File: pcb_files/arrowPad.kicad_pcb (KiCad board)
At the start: 2 copper layers, 43 parts, among them J1 AudioJack3_Ground, J2 AudioJack3_Ground, K1 KEYSW, K10 KEYSW, K11 KEYSW, K12 KEYSW, K13 KEYSW, K14 KEYSW, K15 KEYSW, K16 KEYSW, K2 KEYSW, K3 KEYSW, K4 KEYSW, K5 KEYSW, K6 KEYSW, K7 KEYSW, K8 KEYSW, K9 KEYSW, U1 ProMicro, U2 NRF24L01_Breakout, U3 ADG417BN, U4 AMS1117-3.3, U5 ADG417BN, U6 ADG417BN

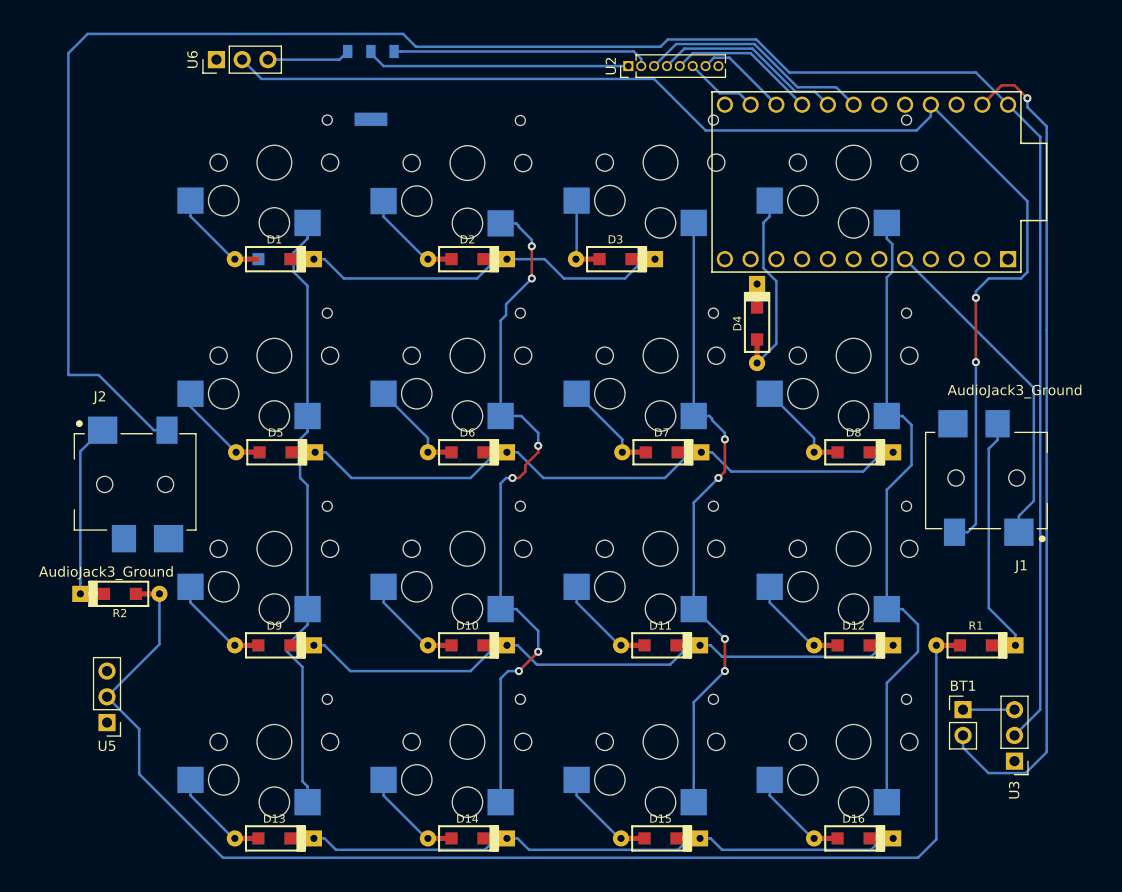
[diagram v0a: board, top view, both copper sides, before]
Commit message: ldo heat sink and edge cuts
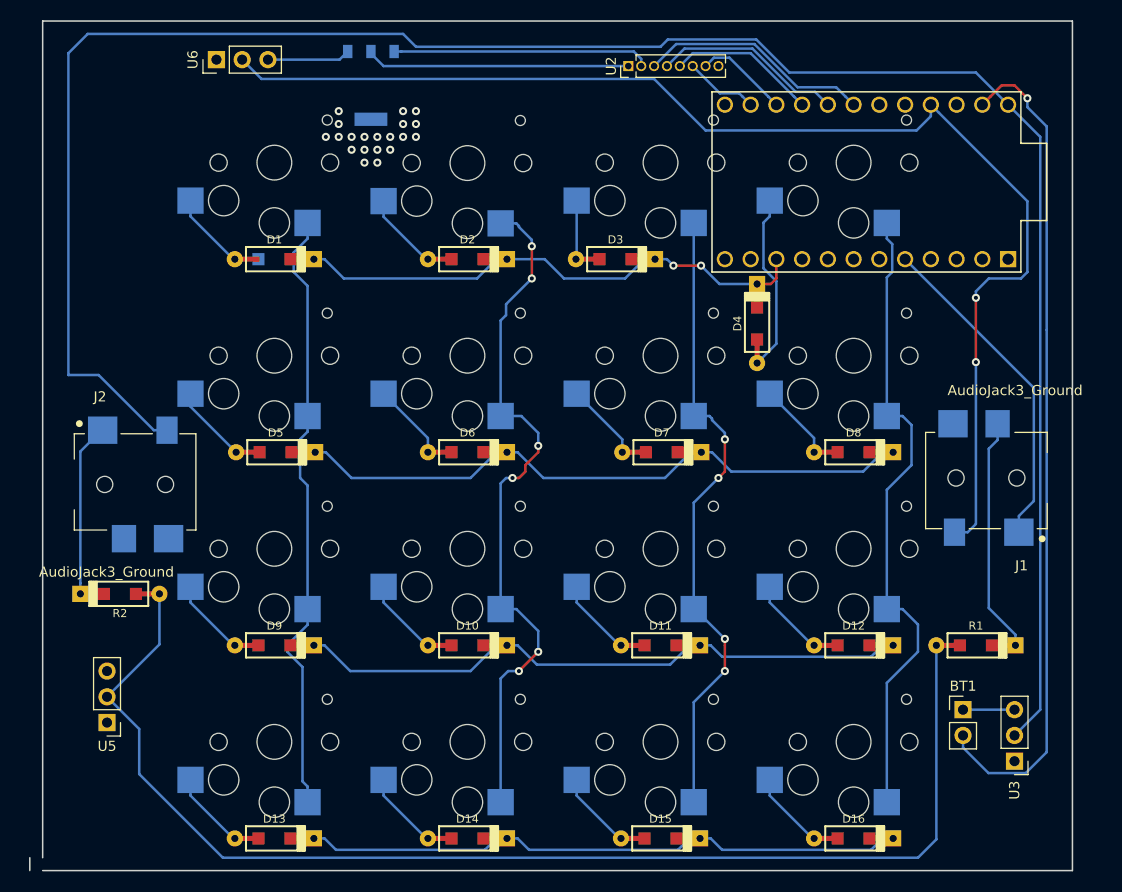
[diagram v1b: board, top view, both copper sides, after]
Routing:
- net /Row1: track 36.8 -> 51.9 mm, vias 0 -> 2
- net (no net): vias 0 -> 20
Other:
- board outline added: 102.9 x 83.8 mm
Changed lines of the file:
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@@
-(kicad_pcb (version 20171130) (host pcbnew "(5.0.0-3-g5ebb6b6)")
+(kicad_pcb (version 20171130) (host pcbnew "(5.0.1)-4")
   (general
     (thickness 1.6)
-    (drawings 0)
-    (tracks 290)
+    (drawings 7)
+    (tracks 321)
     (zones 0)
     (modules 43)
@@
     (pad Hole np_thru_hole circle (at -1.5 0) (size 1.6 1.6) (drill 1.6) (layers *.Cu *.Mask F.SilkS))
   )
+  (dimension 101.6 (width 0.3) (layer Dwgs.User)
+    (gr_text "101.600 mm" (at 158.75 32.19) (layer Dwgs.User)
+      (effects (font (size 1.5 1.5) (thickness 0.3)))
+    )
+    (feature1 (pts (xy 107.95 50.8) (xy 107.95 33.703579)))
+    (feature2 (pts (xy 209.55 50.8) (xy 209.55 33.703579)))
+    (crossbar (pts (xy 209.55 34.29) (xy 107.95 34.29)))
+    (arrow1a (pts (xy 107.95 34.29) (xy 109.076504 33.703579)))
+    (arrow1b (pts (xy 107.95 34.29) (xy 109.076504 34.876421)))
+    (arrow2a (pts (xy 209.55 34.29) (xy 208.423496 33.703579)))
+    (arrow2b (pts (xy 209.55 34.29) (xy 208.423496 34.876421)))
+  )
+  (dimension 83.82 (width 0.3) (layer Dwgs.User)
+    (gr_text "83.820 mm" (at 254.83 92.71 90) (layer Dwgs.User)
+      (effects (font (size 1.5 1.5) (thickness 0.3)))
+    )
+    (feature1 (pts (xy 210.82 50.8) (xy 253.316421 50.8)))
+    (feature2 (pts (xy 210.82 134.62) (xy 253.316421 134.62)))
+    (crossbar (pts (xy 252.73 134.62) (xy 252.73 50.8)))
+    (arrow1a (pts (xy 252.73 50.8) (xy 253.316421 51.926504)))
+    (arrow1b (pts (xy 252.73 50.8) (xy 252.143579 51.926504)))
+    (arrow2a (pts (xy 252.73 134.62) (xy 253.316421 133.493496)))
+    (arrow2b (pts (xy 252.73 134.62) (xy 252.143579 133.493496)))
+  )
+  (gr_line (start 107.95 134.62) (end 209.55 134.62) (layer Edge.Cuts) (width 0.15))
+  (gr_line (start 106.68 133.35) (end 106.68 134.62) (layer Edge.Cuts) (width 0.15))
+  (gr_line (start 209.55 50.8) (end 209.55 134.62) (layer Edge.Cuts) (width 0.15))
+  (gr_line (start 107.95 50.8) (end 209.55 50.8) (layer Edge.Cuts) (width 0.15))
+  (gr_line (start 107.95 133.35) (end 107.95 50.8) (layer Edge.Cuts) (width 0.15))
+  (via (at 143.51 59.69) (size 0.8) (drill 0.4) (layers F.Cu B.Cu) (net 0))
+  (via (at 143.51 60.96) (size 0.8) (drill 0.4) (layers F.Cu B.Cu) (net 0))
+  (via (at 143.51 62.23) (size 0.8) (drill 0.4) (layers F.Cu B.Cu) (net 0))
+  (via (at 142.24 62.23) (size 0.8) (drill 0.4) (layers F.Cu B.Cu) (net 0))
+  (via (at 140.97 62.23) (size 0.8) (drill 0.4) (layers F.Cu B.Cu) (net 0))
+  (via (at 139.7 62.23) (size 0.8) (drill 0.4) (layers F.Cu B.Cu) (net 0))
+  (via (at 138.43 62.23) (size 0.8) (drill 0.4) (layers F.Cu B.Cu) (net 0))
+  (via (at 137.16 62.23) (size 0.8) (drill 0.4) (layers F.Cu B.Cu) (net 0))
+  (via (at 137.16 60.96) (size 0.8) (drill 0.4) (layers F.Cu B.Cu) (net 0))
+  (via (at 137.16 59.69) (size 0.8) (drill 0.4) (layers F.Cu B.Cu) (net 0))
+  (via (at 142.24 63.5) (size 0.8) (drill 0.4) (layers F.Cu B.Cu) (net 0))
+  (via (at 140.97 63.5) (size 0.8) (drill 0.4) (layers F.Cu B.Cu) (net 0))
+  (via (at 139.7 63.5) (size 0.8) (drill 0.4) (layers F.Cu B.Cu) (net 0))
+  (via (at 138.43 63.5) (size 0.8) (drill 0.4) (layers F.Cu B.Cu) (net 0))
+  (via (at 144.78 60.96) (size 0.8) (drill 0.4) (layers F.Cu B.Cu) (net 0))
+  (via (at 144.78 59.69) (size 0.8) (drill 0.4) (layers F.Cu B.Cu) (net 0))
+  (via (at 140.97 64.77) (size 0.8) (drill 0.4) (layers F.Cu B.Cu) (net 0))
+  (via (at 139.7 64.77) (size 0.8) (drill 0.4) (layers F.Cu B.Cu) (net 0))
+  (via (at 144.78 62.23) (size 0.8) (drill 0.4) (layers F.Cu B.Cu) (net 0))
+  (via (at 135.89 62.23) (size 0.8) (drill 0.4) (layers F.Cu B.Cu) (net 0))
   (segment (start 118.92 91.17) (end 120.22 91.17) (width 0.25) (layer B.Cu) (net 1))
   (segment (start 113.475 85.725) (end 118.92 91.17) (width 0.25) (layer B.Cu) (net 1))
@@
   (segment (start 150.805 76.2) (end 152.71 74.295) (width 0.25) (layer B.Cu) (net 4))
   (segment (start 137.665 76.2) (end 150.805 76.2) (width 0.25) (layer B.Cu) (net 4))
+  (segment (start 168.365 74.295) (end 169.545 74.295) (width 0.25) (layer B.Cu) (net 4))
+  (via (at 170.18 74.93) (size 0.8) (drill 0.4) (layers F.Cu B.Cu) (net 4))
+  (segment (start 169.545 74.295) (end 170.18 74.93) (width 0.25) (layer B.Cu) (net 4))
+  (segment (start 170.18 74.93) (end 172.72 74.93) (width 0.25) (layer F.Cu) (net 4))
+  (via (at 172.91 74.93) (size 0.8) (drill 0.4) (layers F.Cu B.Cu) (net 4))
+  (segment (start 172.72 74.93) (end 172.91 74.93) (width 0.25) (layer F.Cu) (net 4))
+  (segment (start 174.725 76.745) (end 178.435 76.745) (width 0.25) (layer B.Cu) (net 4))
+  (segment (start 172.91 74.93) (end 174.725 76.745) (width 0.25) (layer B.Cu) (net 4))
+  (segment (start 178.435 76.745) (end 179.795 76.745) (width 0.25) (layer F.Cu) (net 4))
+  (segment (start 180.34 76.2) (end 180.34 74.295) (width 0.25) (layer F.Cu) (net 4))
+  (segment (start 179.795 76.745) (end 180.34 76.2) (width 0.25) (layer F.Cu) (net 4))
   (segment (start 141.585 70.114) (end 145.766 74.295) (width 0.25) (layer B.Cu) (net 5))
   (segment (start 145.766 74.295) (end 145.96 74.295) (width 0.25) (layer B.Cu) (net 5))

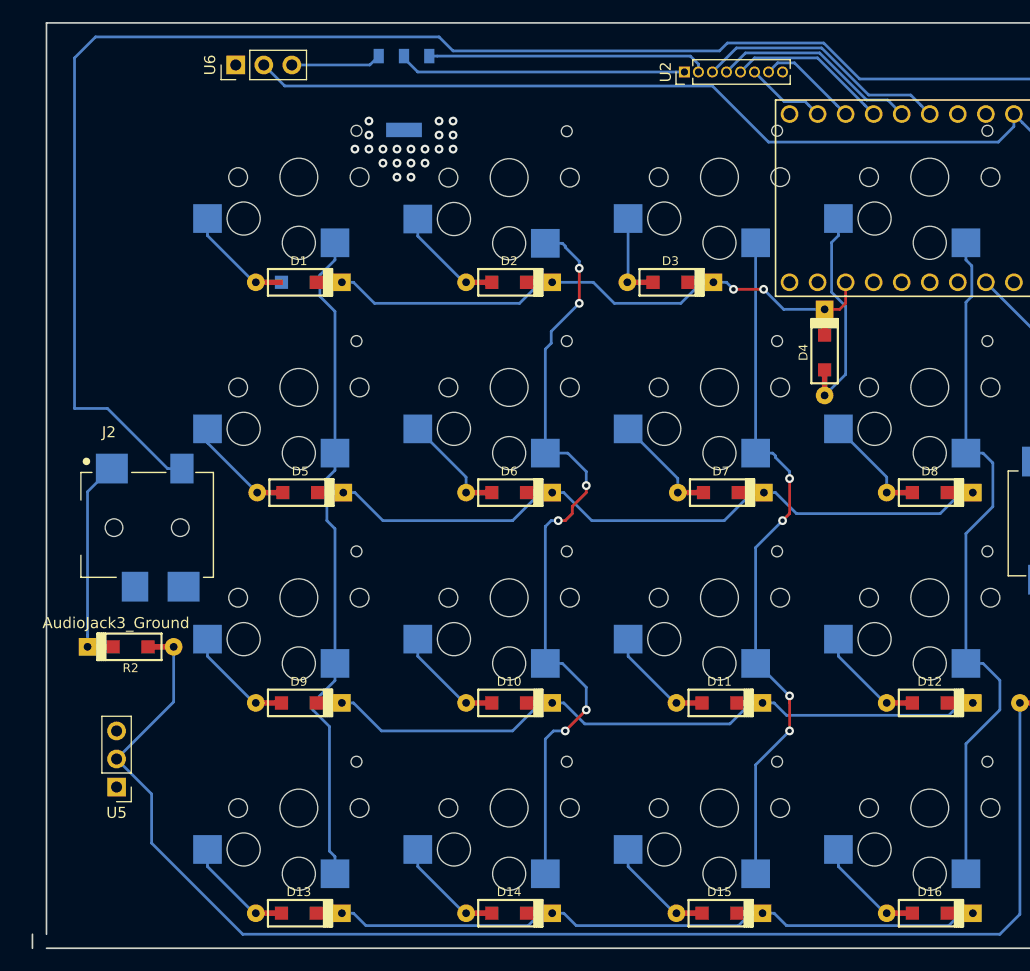
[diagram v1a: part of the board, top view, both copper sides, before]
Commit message: TLC5940 LED controller
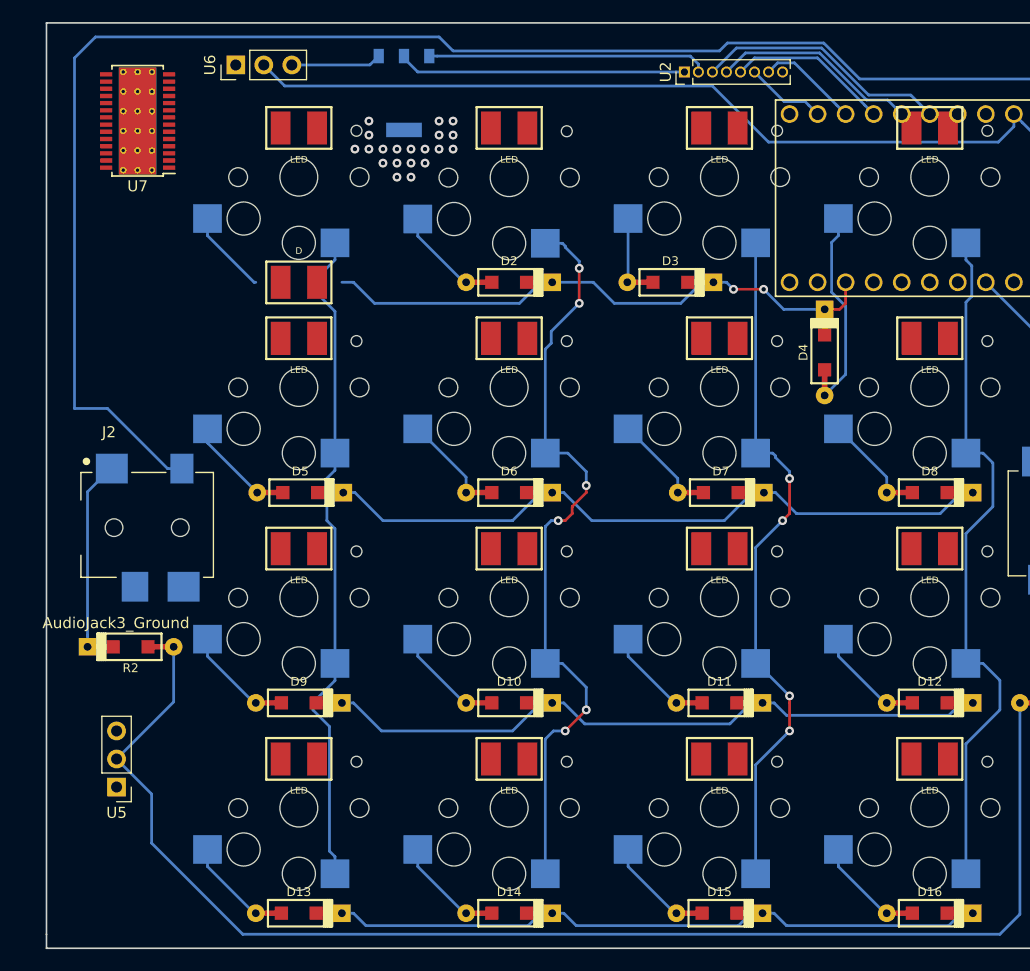
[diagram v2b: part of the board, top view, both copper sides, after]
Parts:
- added D20: LED, keyboard_parts:C_3528, F.Cu at (130.8, 60.3)
- added D21: LED, keyboard_parts:C_3528, F.Cu at (149.9, 60.3)
- added D22: LED, keyboard_parts:C_3528, F.Cu at (168.9, 60.3)
- added D23: LED, keyboard_parts:C_3528, F.Cu at (188.0, 60.3)
- added D24: LED, keyboard_parts:C_3528, F.Cu at (130.8, 79.4)
- added D25: LED, keyboard_parts:C_3528, F.Cu at (149.9, 79.4)
- added D26: LED, keyboard_parts:C_3528, F.Cu at (168.9, 79.4)
- added D27: LED, keyboard_parts:C_3528, F.Cu at (188.0, 79.4)
- added D28: LED, keyboard_parts:C_3528, F.Cu at (130.8, 98.4)
- added D29: LED, keyboard_parts:C_3528, F.Cu at (149.9, 98.4)
- added D30: LED, keyboard_parts:C_3528, F.Cu at (168.9, 98.4)
- added D31: LED, keyboard_parts:C_3528, F.Cu at (188.0, 98.4)
- added D32: LED, keyboard_parts:C_3528, F.Cu at (130.8, 117.5)
- added D33: LED, keyboard_parts:C_3528, F.Cu at (149.9, 117.5)
- added D34: LED, keyboard_parts:C_3528, F.Cu at (168.9, 117.5)
- added D35: LED, keyboard_parts:C_3528, F.Cu at (188.0, 117.5)
- added U7: TLC5940PWP, Package_SO:HTSSOP-28-1EP_4.4x9.7mm_P0.65mm_EP3.4x9.5mm_Mask2.4x6.17mm_ThermalVias, F.Cu at (116.2, 59.7)
- D1: footprint keyboard_parts:D_SOD123_axial -> keyboard_parts:C_3528
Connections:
- U1 pad 1: Net-(U1-Pad1) -> /Col2
- U1 pad 13: /Row3 -> Net-(U1-Pad13)
- U1 pad 2: Net-(U1-Pad2) -> /Row3
- U1 pad 8: /Col2 -> /GSCLK
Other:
- board size 102.9 x 83.8 mm -> 101.6 x 83.8 mm

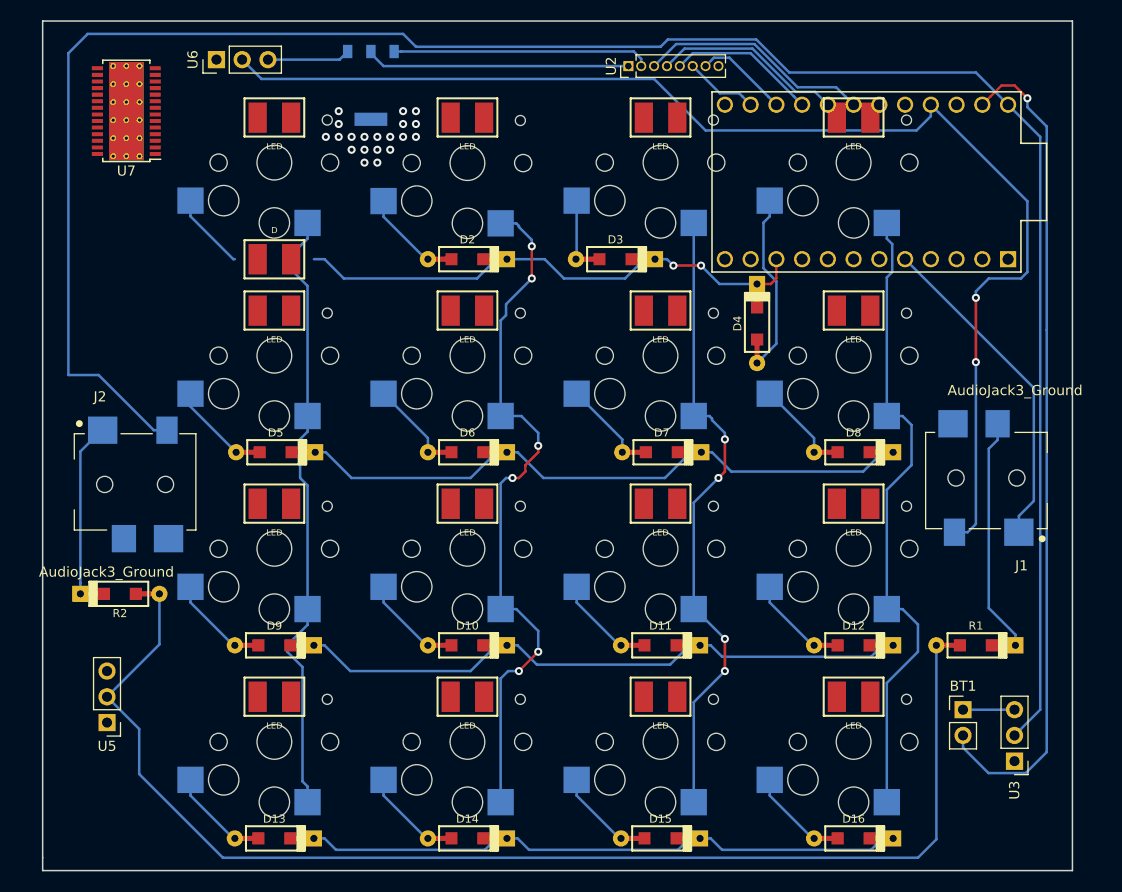
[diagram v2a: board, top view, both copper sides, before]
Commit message: traces from led ic
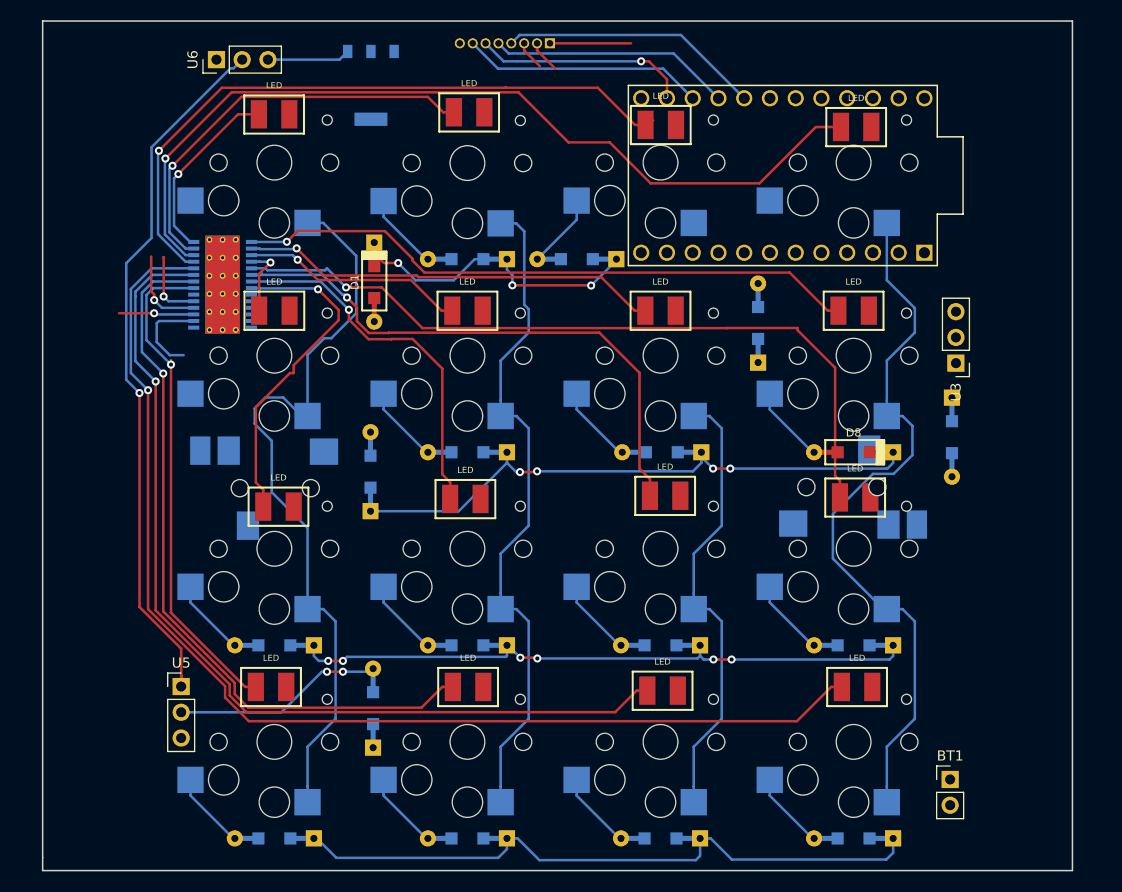
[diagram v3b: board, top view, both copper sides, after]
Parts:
- D1: footprint keyboard_parts:C_3528 -> keyboard_parts:D_SOD123_axial
- D10, D11, D12, D13, D14, D15, D16, D2, D3, D4, D5, D6, D7, D9, R1, R2, U2, U7: moved to B.Cu
- D20, D21, D22, D23, D24, D25, D26, D27, D28, D29, D30, D31, D32, D33, D34, D35: footprint keyboard_parts:C_3528 -> foots:C_3528v1
- J1, J2: footprint foots:CUI_SJ1-3514-SMT[PAD1,2,34]Backside -> SJ-43514-SMT:CUI_SJ-43514-SMT; moved to B.Cu
- moved D32 57.5 mm to (188.3, 116.5), turned to 180 degrees
- moved D35 57.5 mm to (130.5, 116.5), turned to 180 degrees
- moved D31 41.9 mm to (168.9, 61.0), turned to 180 degrees
- moved D30 41.9 mm to (188.2, 61.3), turned to 180 degrees
- moved U3 39.7 mm to (198.1, 84.6)
- moved D29 38.6 mm to (150.0, 59.8), turned to 180 degrees
- moved D28 38.4 mm to (130.8, 60.0), turned to 180 degrees
- moved D20 38.4 mm to (131.2, 98.7), turned to 180 degrees
- moved D21 37.6 mm to (149.7, 98.0), turned to 180 degrees
- moved D23 37.5 mm to (188.1, 97.8), turned to 180 degrees
- moved D22 37.3 mm to (169.4, 97.6), turned to 180 degrees
- moved R2 27.4 mm to (140.6, 118.6), turned to 90 degrees
- moved R1 20.7 mm to (197.7, 91.9), turned to 270 degrees
- moved U7 19.6 mm to (125.7, 76.8), turned to 0 degrees
- moved D33 19.3 mm to (169.1, 116.9), turned to 180 degrees
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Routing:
- net /RAW1: track 205.3 -> 0.00 mm
- net Net-(D32-Pad2): track 0.00 -> 114.4 mm, vias 0 -> 1
- net /GND1: track 107.8 -> 3.97 mm, vias 1 -> 0
- net Net-(R1-Pad2): track 123.2 -> 20.7 mm, vias 0 -> 2
- net Net-(D33-Pad2): track 0.00 -> 92.9 mm, vias 0 -> 1
- net Net-(D30-Pad2): track 0.00 -> 86.6 mm, vias 0 -> 1
- net Net-(D23-Pad2): track 0.00 -> 74.9 mm, vias 0 -> 1
- net Net-(D34-Pad2): track 0.00 -> 71.9 mm, vias 0 -> 1
- net Net-(D31-Pad2): track 0.00 -> 66.1 mm, vias 0 -> 1
- net Net-(D27-Pad2): track 0.00 -> 61.7 mm, vias 0 -> 1
- net Net-(D22-Pad2): track 0.00 -> 56.7 mm, vias 0 -> 1
- net /VCC1: track 124.3 -> 70.1 mm, vias 2 -> 1
- net Net-(J1-Pad1): track 49.9 -> 0.00 mm
- net Net-(D35-Pad2): track 0.00 -> 49.2 mm, vias 0 -> 1
- net Net-(D26-Pad2): track 0.00 -> 41.5 mm, vias 0 -> 1
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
